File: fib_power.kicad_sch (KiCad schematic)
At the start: 32 parts, among them U201 TLV75718PDBV, U202 TLV75733PDBV, U203 TPS61022RWUR, U204 TPS56428DDA

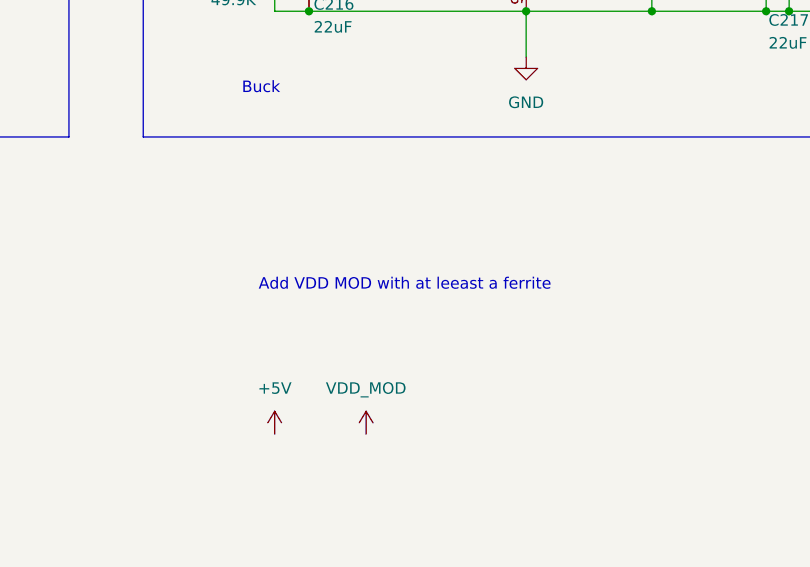
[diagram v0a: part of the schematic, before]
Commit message: added connections to ESP32 S3, most oof EPD stuff that we're gooing to use is included
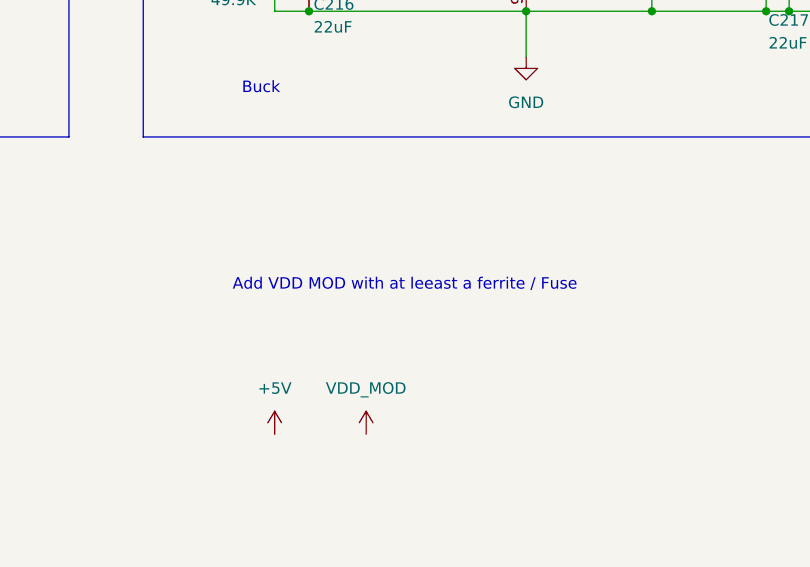
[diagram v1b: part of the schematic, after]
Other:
- note added: "Add VDD MOD with at leeast a ferrite / Fuse"
- note removed: "Add VDD MOD with at leeast a ferrite"
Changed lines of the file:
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@@
 		)
 	)
-	(text "Add VDD MOD with at leeast a ferrite"
+	(text "Add VDD MOD with at leeast a ferrite / Fuse"
 		(exclude_from_sim no)
 		(at 170.688 80.01 0)

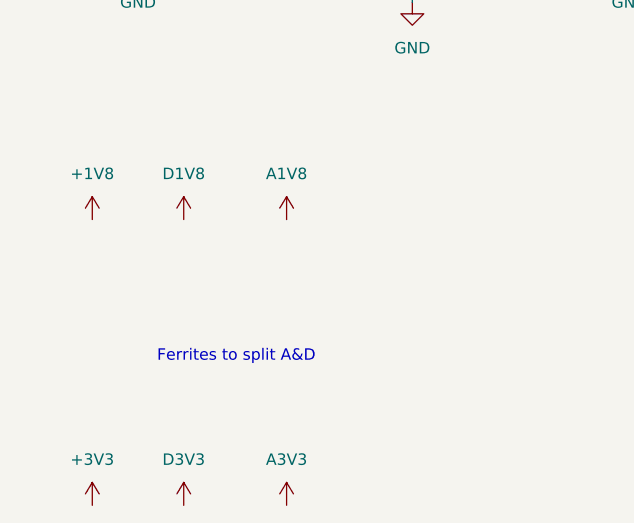
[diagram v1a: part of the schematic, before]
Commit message: refactored PCIe pages
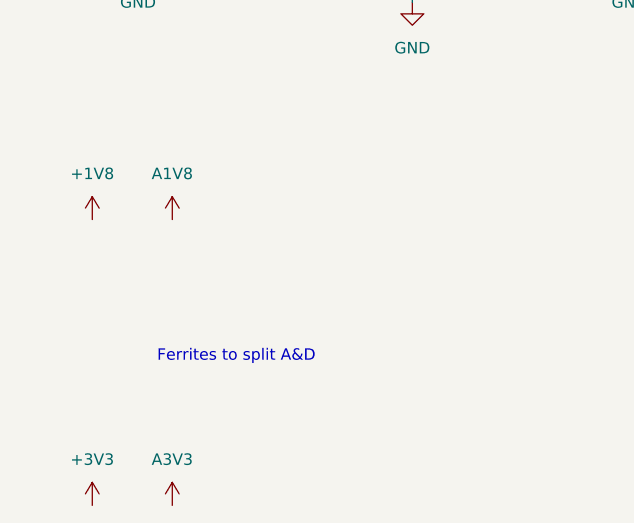
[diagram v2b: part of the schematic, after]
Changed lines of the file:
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@@
 	(symbol
 		(lib_id "power:+3.3V")
-		(at 46.99 148.59 0)
+		(at 34.29 148.59 0)
 		(unit 1)
 		(exclude_from_sim no)
@@
 		(fields_autoplaced yes)
 		(property "Reference" "#PWR0211"
-			(at 46.99 152.4 0)
+			(at 34.29 152.4 0)
 			(effects
 				(font
@@
 		)
 		(property "Value" "A1V8"
-			(at 46.99 143.51 0)
+			(at 34.29 143.51 0)
 			(effects
 				(font
@@
 		)
 		(property "Footprint" ""
-			(at 46.99 148.59 0)
+			(at 34.29 148.59 0)
 			(effects
 				(font
@@
 		)
 		(property "Datasheet" ""
-			(at 46.99 148.59 0)
+			(at 34.29 148.59 0)
 			(effects
 				(font
@@
 		)
 		(property "Description" "Power symbol creates a global label with name \"+3.3V\""
-			(at 46.99 148.59 0)
+			(at 34.29 148.59 0)
 			(effects
 				(font
@@
 	)
 	(symbol
-		(lib_id "power:+3.3V")
-		(at 35.56 148.59 0)
-		(unit 1)
-		(exclude_from_sim no)
-		(in_bom yes)
-		(on_board yes)
-		(dnp no)
-		(fields_autoplaced yes)
-		(property "Reference" "#PWR0207"
-			(at 35.56 152.4 0)
-			(effects
-				(font
-					(size 1.27 1.27)
-				)
-				(hide yes)
-			)
-		)
-		(property "Value" "D1V8"
-			(at 35.56 143.51 0)
-			(effects
-				(font
-					(size 1.27 1.27)
-				)
-			)
-		)
-		(property "Footprint" ""
-			(at 35.56 148.59 0)
-			(effects
-				(font
-					(size 1.27 1.27)
-				)
-				(hide yes)
-			)
-		)
-		(property "Datasheet" ""
-			(at 35.56 148.59 0)
-			(effects
-				(font
-					(size 1.27 1.27)
-				)
-				(hide yes)
-			)
-		)
-		(property "Description" "Power symbol creates a global label with name \"+3.3V\""
-			(at 35.56 148.59 0)
-			(effects
-				(font
-					(size 1.27 1.27)
-				)
-				(hide yes)
-			)
-		)
-		(pin "1"
-		)
-		(instances
-			(project "Fibel2"
-				(path "/862c21e2-7ec9-4f80-a33c-aad02ea9423e/7cbf83a4-48a9-4119-ac75-03df93e67514"
-					(reference "#PWR0207")
-					(unit 1)
-				)
-			)
-		)
-	)
-	(symbol
 		(lib_id "Device:C_Small")
 		(at 85.09 114.3 0)
@@
 	(symbol
 		(lib_id "power:+3.3V")
-		(at 35.56 180.34 0)
-		(unit 1)
-		(exclude_from_sim no)
-		(in_bom yes)
-		(on_board yes)
-		(dnp no)
-		(fields_autoplaced yes)
-		(property "Reference" "#PWR0208"
-			(at 35.56 184.15 0)
-			(effects
-				(font
-					(size 1.27 1.27)
-				)
-				(hide yes)
-			)
-		)
-		(property "Value" "D3V3"
-			(at 35.56 175.26 0)
-			(effects
-				(font
-					(size 1.27 1.27)
-				)
-			)
-		)
-		(property "Footprint" ""
-			(at 35.56 180.34 0)
-			(effects
-				(font
-					(size 1.27 1.27)
-				)
-				(hide yes)
-			)
-		)
-		(property "Datasheet" ""
-			(at 35.56 180.34 0)
-			(effects
-				(font
-					(size 1.27 1.27)
-				)
-				(hide yes)
-			)
-		)
-		(property "Description" "Power symbol creates a global label with name \"+3.3V\""
-			(at 35.56 180.34 0)
-			(effects
-				(font
-					(size 1.27 1.27)
-				)
-				(hide yes)
-			)
-		)
-		(pin "1"
-		)
-		(instances
-			(project "Fibel2"
-				(path "/862c21e2-7ec9-4f80-a33c-aad02ea9423e/7cbf83a4-48a9-4119-ac75-03df93e67514"
-					(reference "#PWR0208")
-					(unit 1)
-				)
-			)
-		)
-	)
-	(symbol
-		(lib_id "power:+3.3V")
-		(at 46.99 180.34 0)
+		(at 34.29 180.34 0)
 		(unit 1)
 		(exclude_from_sim no)
@@
 		(fields_autoplaced yes)
 		(property "Reference" "#PWR0212"
-			(at 46.99 184.15 0)
+			(at 34.29 184.15 0)
 			(effects
 				(font
@@
 		)
 		(property "Value" "A3V3"
-			(at 46.99 175.26 0)
+			(at 34.29 175.26 0)
 			(effects
 				(font
@@
 		)
 		(property "Footprint" ""
-			(at 46.99 180.34 0)
+			(at 34.29 180.34 0)
 			(effects
 				(font
@@
 		)
 		(property "Datasheet" ""
-			(at 46.99 180.34 0)
+			(at 34.29 180.34 0)
 			(effects
 				(font
@@
 		)
 		(property "Description" "Power symbol creates a global label with name \"+3.3V\""
-			(at 46.99 180.34 0)
+			(at 34.29 180.34 0)
 			(effects
 				(font

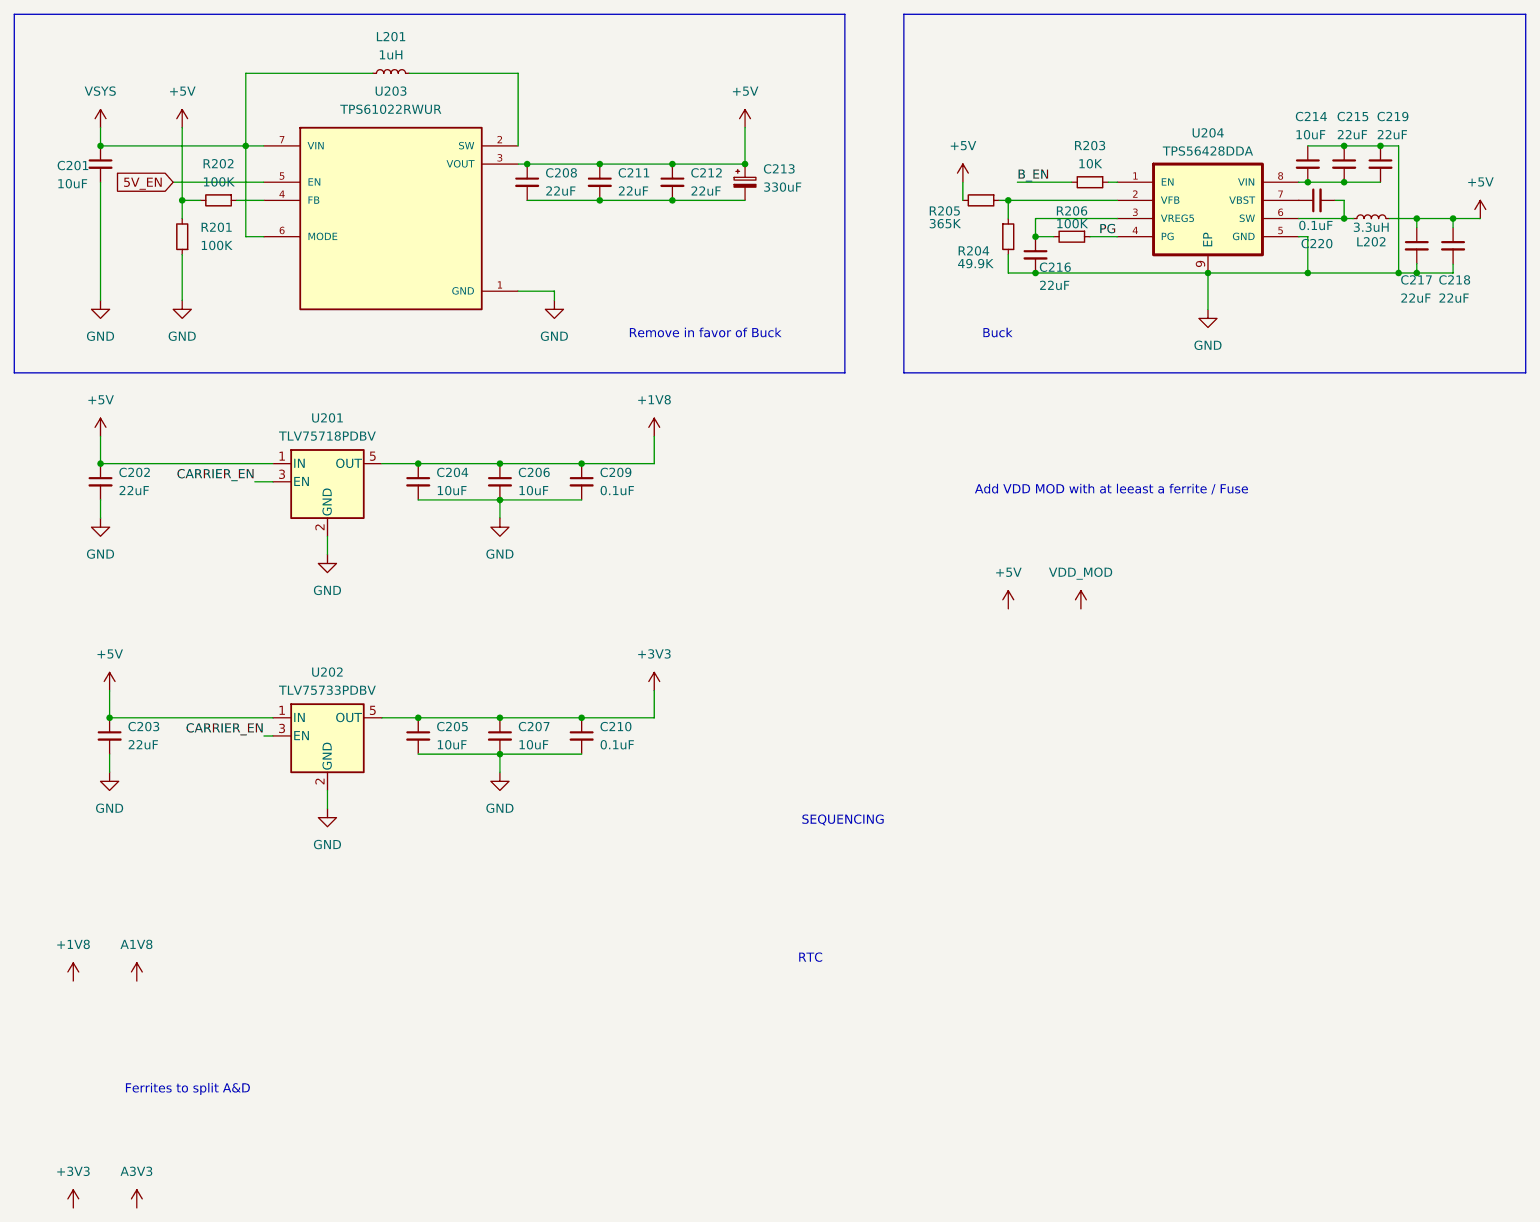
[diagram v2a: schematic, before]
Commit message: added some missing footprints, stared working ono power-on and sequencing
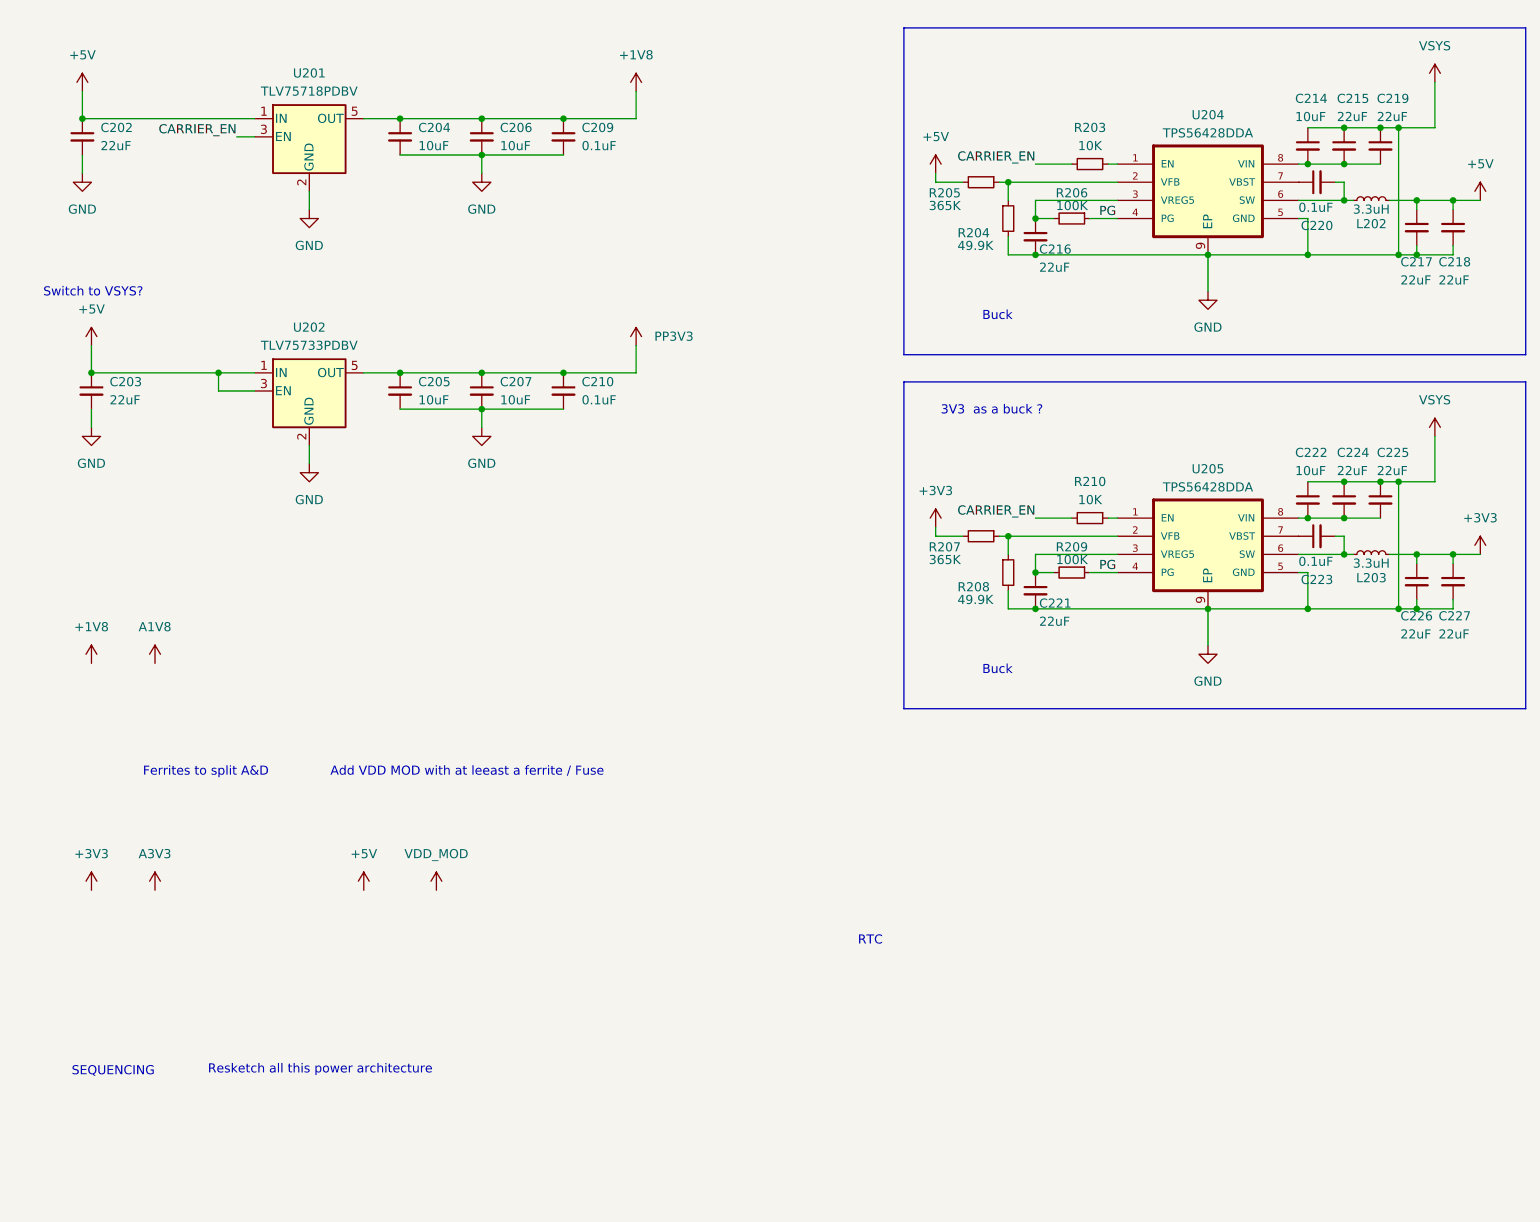
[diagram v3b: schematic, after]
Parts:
- removed C201: 10uF, Capacitor_SMD:C_0603_1608Metric, symbol Device:C_Small
- removed C208, C211, C212: 22uF, Capacitor_SMD:C_0805_2012Metric, symbol Device:C_Small
- removed C213: 330uF, Capacitor_Tantalum_SMD:CP_EIA-6032-15_Kemet-U, symbol Device:C_Polarized_Small
- removed L201: 1uH, symbol Device:L_Small
- removed R201, R202: 100K, Resistor_SMD:R_0603_1608Metric, symbol Device:R_Small
- removed U203: TPS61022RWUR, Fibel2:TPS61022RWUR, symbol Fibel2:TPS61022RWUR
- added C221, C224, C225, C227: 22uF, Capacitor_SMD:C_0805_2012Metric, symbol Device:C_Small
- added C222: 10uF, Capacitor_SMD:C_0603_1608Metric, symbol Device:C_Small
- added C223: 0.1uF, Capacitor_SMD:C_0805_2012Metric, symbol Device:C_Small
- added C226: 22uF, Capacitor_SMD:C_0603_1608Metric, symbol Device:C_Small
- added L203: 3.3uH, symbol Device:L_Small
- added R207: 365K, Resistor_SMD:R_0603_1608Metric, symbol Device:R_Small
- added R208: 49.9K, Resistor_SMD:R_0603_1608Metric, symbol Device:R_Small
- added R209: 100K, Resistor_SMD:R_0603_1608Metric, symbol Device:R_Small
- added R210: 10K, Resistor_SMD:R_0603_1608Metric, symbol Device:R_Small
- added U205: TPS56428DDA, Fibel2:TPS56428DDA, symbol Fibel2:TPS56428DDA
- L202: footprint (none) -> Resistor_SMD:R_0603_1608Metric
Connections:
- net B_EN is gone; now on net CARRIER_EN: R203.2
- net +3V3: now also C226.1, C227.1, L203.2, R207.2; no longer C205.1, C207.1, C210.1, U202.5 (OUT)
- net +5V: now also U202.3 (EN)
- net CARRIER_EN: now also R210.2; no longer U202.3 (EN)
- net GND: now also C221.2, C222.1, C224.1, C225.1, C226.2, C227.2, R208.2, U205.5 (GND), U205.9 (EP)
- net PG: now also R209.1, U205.4 (PG)
- new net: R207.1, R208.1, U205.2 (VFB)
- new net: R210.1, U205.1 (EN)
- new net: C222.2, C224.2, C225.2, U205.8 (VIN)
- new net: C221.1, R209.2, U205.3 (VREG5)
- new net: C223.2, L203.1, U205.6 (SW)
- new net: C223.1, U205.7 (VBST)
- new net PP3V3: C205.1, C207.1, C210.1, U202.5 (OUT)
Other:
- note added: "3V3 as a buck ?"
- note added: "Resketch all this power architecture"
- note added: "Switch to VSYS?"
- note removed: "Remove in favor of Buck"
- moved on the sheet: C202, C203, C204, C205, C206, C207, C209, C210, C214, C215, C216, C217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
